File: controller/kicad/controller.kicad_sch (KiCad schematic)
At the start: 28 parts, among them J1 pcie_98, U1 WeAct_STM32H750_Module, U10 ESD5344D, U11 ESD5344D, U12 ESD5344D, U13 ESD5344D, U14 ESD5344D, U15 ESD5344D, U16 ESD5344D, U17 ESD5344D, U18 ESD5344D, U19 ESD5344D, U2 ESD5344D, U20 ESD5344D, U21 ESD5344D, U3 ESD5344D, U4 ESD5344D, U5 ESD5344D, U6 ESD5344D, U7 ESD5344D, U8 ESD5344D, U9 ESD5344D

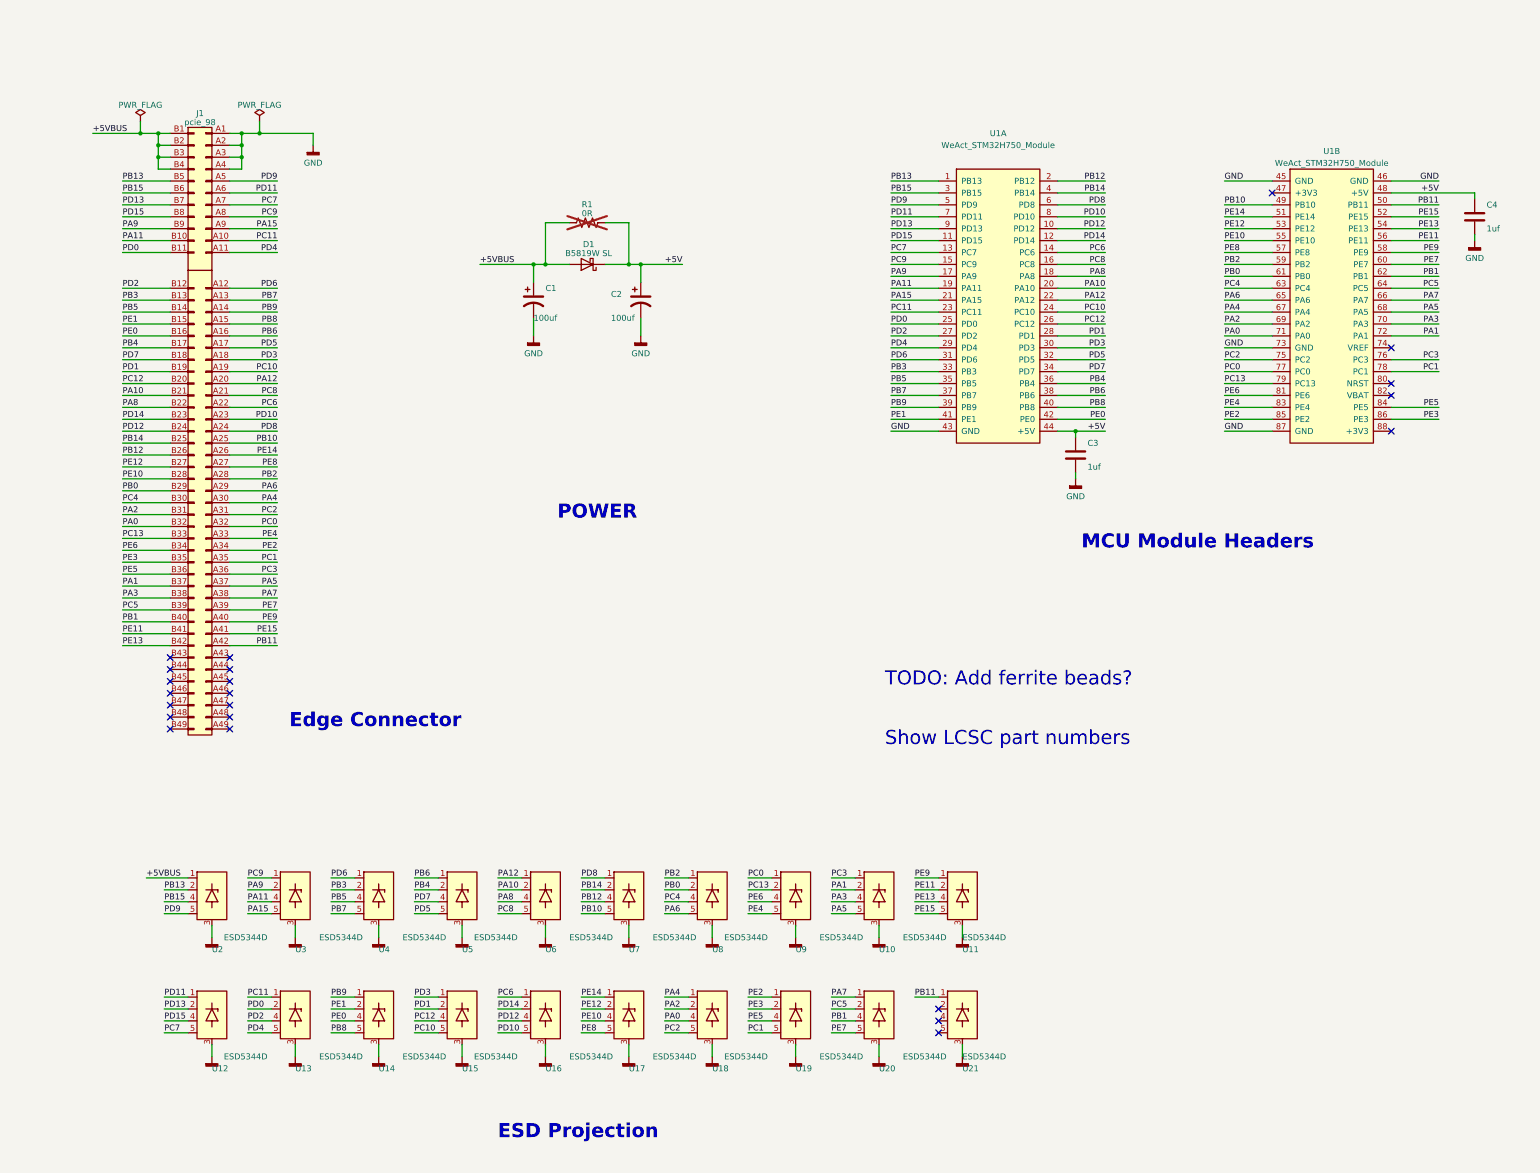
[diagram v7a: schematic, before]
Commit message: Exposed the LCSC numbers in the Controller's schematic.
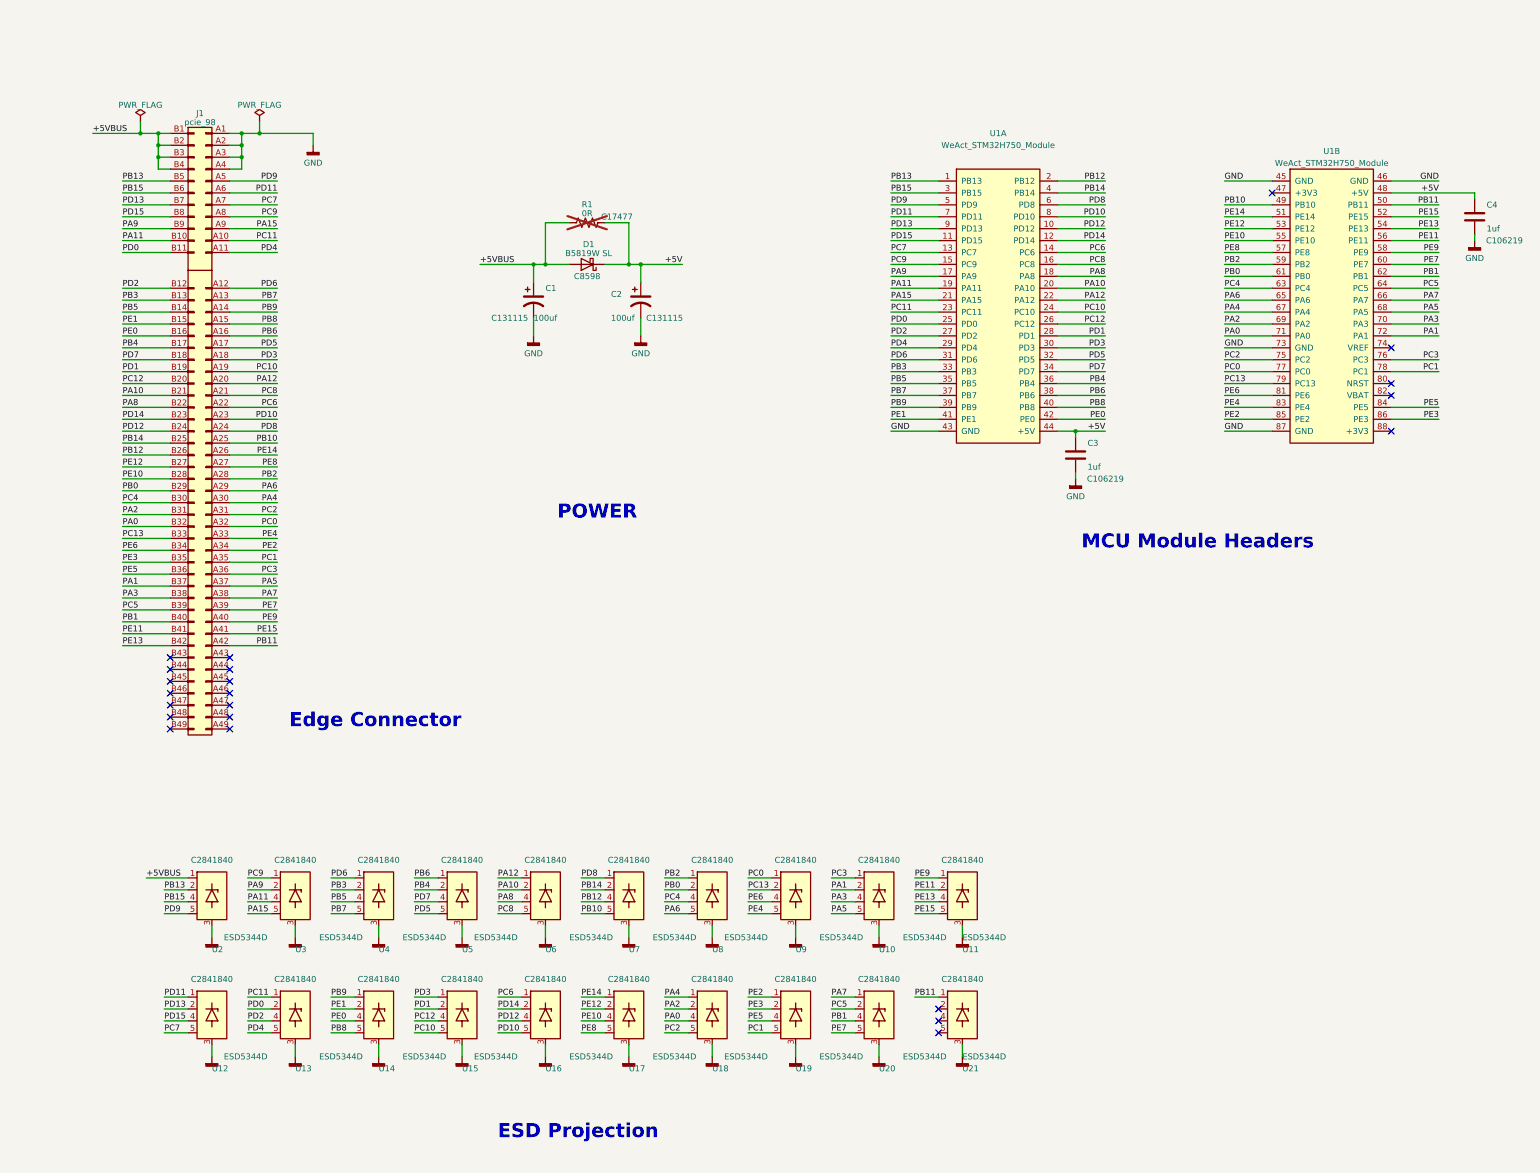
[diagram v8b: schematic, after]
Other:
- note removed: "Show LCSC part numbers"
- note removed: "TODO: Add ferrite beads?"
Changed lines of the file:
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@@
     (effects (font (size 3 3) (thickness 0.6) bold) (justify left bottom))
-  )
-  (text "Show LCSC part numbers" (at 238.76 176.53 0)
-    (effects (font (size 3 3) (color 255 0 0 1)) (justify left bottom))
-  )
-  (text "TODO: Add ferrite beads?" (at 238.76 163.83 0)
-    (effects (font (size 3 3) (color 255 0 0 1)) (justify left bottom))
   )
   (text "MCU Module Headers" (at 280.67 134.62 0)
@@
       (effects (font (size 1.27 1.27)) hide)
     )
-    (property "LCSC" "C2841840" (at 255.27 234.95 0)
-      (effects (font (size 1.27 1.27)) hide)
+    (property "LCSC" "C2841840" (at 255.27 226.06 0)
+      (effects (font (size 1.27 1.27)))
     )
     (pin "1")
@@
       (effects (font (size 1.27 1.27)) hide)
     )
-    (property "LCSC" "C106219" (at 279.4 114.3 0)
-      (effects (font (size 1.27 1.27)) hide)
+    (property "LCSC" "C106219" (at 285.75 119.38 0)
+      (effects (font (size 1.27 1.27)))
     )
     (pin "1")
@@
       (effects (font (size 1.27 1.27)) hide)
     )
-    (property "LCSC" "C2841840" (at 201.93 209.55 0)
-      (effects (font (size 1.27 1.27)) hide)
+    (property "LCSC" "C2841840" (at 201.93 200.66 0)
+      (effects (font (size 1.27 1.27)))
     )
     (pin "1")
@@
       (effects (font (size 1.27 1.27)) hide)
     )
-    (property "LCSC" "C2841840" (at 237.49 234.95 0)
-      (effects (font (size 1.27 1.27)) hide)
+    (property "LCSC" "C2841840" (at 237.49 226.06 0)
+      (effects (font (size 1.27 1.27)))
     )
     (pin "1")
@@
       (effects (font (size 1.27 1.27)) hide)
     )
-    (property "LCSC" "C2841840" (at 219.71 209.55 0)
-      (effects (font (size 1.27 1.27)) hide)
+    (property "LCSC" "C2841840" (at 219.71 200.66 0)
+      (effects (font (size 1.27 1.27)))
     )
     (pin "1")
@@
       (effects (font (size 1.27 1.27)) hide)
     )
-    (property "LCSC" "C2841840" (at 219.71 234.95 0)
-      (effects (font (size 1.27 1.27)) hide)
+    (property "LCSC" "C2841840" (at 219.71 226.06 0)
+      (effects (font (size 1.27 1.27)))
     )
     (pin "1")
@@
       (effects (font (size 1.27 1.27)) hide)
     )
-    (property "LCSC" "C131115" (at 163.83 81.28 0)
-      (effects (font (size 1.27 1.27)) hide)
+    (property "LCSC" "C131115" (at 158.75 85.09 0)
+      (effects (font (size 1.27 1.27)))
     )
     (pin "1")
@@
       (effects (font (size 1.27 1.27)) hide)
     )
-    (property "LCSC" "C2841840" (at 113.03 209.55 0)
-      (effects (font (size 1.27 1.27)) hide)
+    (property "LCSC" "C2841840" (at 113.03 200.66 0)
+      (effects (font (size 1.27 1.27)))
     )
     (pin "1")
@@
       (effects (font (size 1.27 1.27)) hide)
     )
-    (property "LCSC" "C2841840" (at 201.93 234.95 0)
-      (effects (font (size 1.27 1.27)) hide)
+    (property "LCSC" "C2841840" (at 201.93 226.06 0)
+      (effects (font (size 1.27 1.27)))
     )
     (pin "1")
@@
       (effects (font (size 1.27 1.27)) hide)
     )
-    (property "LCSC" "C2841840" (at 255.27 209.55 0)
-      (effects (font (size 1.27 1.27)) hide)
+    (property "LCSC" "C2841840" (at 255.27 200.66 0)
+      (effects (font (size 1.27 1.27)))
     )
     (pin "1")
@@
       (effects (font (size 1.27 1.27)) hide)
     )
-    (property "LCSC" "C2841840" (at 95.25 209.55 0)
-      (effects (font (size 1.27 1.27)) hide)
+    (property "LCSC" "C2841840" (at 95.25 200.66 0)
+      (effects (font (size 1.27 1.27)))
     )
     (pin "1")
@@
       (effects (font (size 1.27 1.27)) hide)
     )
-    (property "LCSC" "C2841840" (at 95.25 234.95 0)
-      (effects (font (size 1.27 1.27)) hide)
+    (property "LCSC" "C2841840" (at 95.25 226.06 0)
+      (effects (font (size 1.27 1.27)))
     )
     (pin "1")
@@
       (effects (font (size 1.27 1.27)) hide)
     )
-    (property "LCSC" "C2841840" (at 184.15 209.55 0)
-      (effects (font (size 1.27 1.27)) hide)
+    (property "LCSC" "C2841840" (at 184.15 200.66 0)
+      (effects (font (size 1.27 1.27)))
     )
     (pin "1")
@@
   )
   (symbol (lib_id "Device:D_Schottky") (at 175.26 73.66 180) (unit 1)
-    (in_bom yes) (on_board yes) (dnp no) (fields_autoplaced)
+    (in_bom yes) (on_board yes) (dnp no)
     (property "Reference" "D1" (at 175.5775 69.3801 0)
       (effects (font (size 1.27 1.27)))
@@
       (effects (font (size 1.27 1.27)) hide)
     )
-    (property "LCSC" "C8598" (at 175.26 73.66 0)
-      (effects (font (size 1.27 1.27)) hide)
+    (property "LCSC" "C8598" (at 175.26 76.2 0)
+      (effects (font (size 1.27 1.27)))
     )
     (pin "1")
@@
       (effects (font (size 1.27 1.27)) hide)
     )
-    (property "LCSC" "C2841840" (at 237.49 209.55 0)
-      (effects (font (size 1.27 1.27)) hide)
+    (property "LCSC" "C2841840" (at 237.49 200.66 0)
+      (effects (font (size 1.27 1.27)))
     )
     (pin "1")
@@
       (effects (font (size 1.27 1.27)) hide)
     )
-    (property "LCSC" "C2841840" (at 130.81 209.55 0)
-      (effects (font (size 1.27 1.27)) hide)
+    (property "LCSC" "C2841840" (at 130.81 200.66 0)
+      (effects (font (size 1.27 1.27)))
     )
     (pin "1")
@@
       (effects (font (size 1.27 1.27)) hide)
     )
-    (property "LCSC" "C106219" (at 364.49 63.5 0)
-      (effects (font (size 1.27 1.27)) hide)
+    (property "LCSC" "C106219" (at 370.84 68.58 0)
+      (effects (font (size 1.27 1.27)))
     )
     (pin "1")
@@
       (effects (font (size 1.27 1.27)) hide)
     )
-    (property "LCSC" "C2841840" (at 113.03 234.95 0)
-      (effects (font (size 1.27 1.27)) hide)
+    (property "LCSC" "C2841840" (at 113.03 226.06 0)
+      (effects (font (size 1.27 1.27)))
     )
     (pin "1")
@@
       (effects (font (size 1.27 1.27)) hide)
     )
-    (property "LCSC" "C2841840" (at 148.59 234.95 0)
-      (effects (font (size 1.27 1.27)) hide)
+    (property "LCSC" "C2841840" (at 148.59 226.06 0)
+      (effects (font (size 1.27 1.27)))
     )
     (pin "1")
@@
       (effects (font (size 1.27 1.27)) hide)
     )
-    (property "LCSC" "C2841840" (at 148.59 209.55 0)
-      (effects (font (size 1.27 1.27)) hide)
+    (property "LCSC" "C2841840" (at 148.59 200.66 0)
+      (effects (font (size 1.27 1.27)))
     )
     (pin "1")
@@
       (effects (font (size 1.27 1.27)) hide)
     )
-    (property "LCSC" "C2841840" (at 130.81 234.95 0)
-      (effects (font (size 1.27 1.27)) hide)
+    (property "LCSC" "C2841840" (at 130.81 226.06 0)
+      (effects (font (size 1.27 1.27)))
     )
     (pin "1")
@@
   )
   (symbol (lib_id "Device:R_US") (at 175.26 64.77 90) (unit 1)
-    (in_bom no) (on_board yes) (dnp yes) (fields_autoplaced)
+    (in_bom no) (on_board yes) (dnp yes)
     (property "Reference" "R1" (at 175.26 60.8711 90)
       (effects (font (size 1.27 1.27)))
@@
       (effects (font (size 1.27 1.27)) hide)
     )
-    (property "LCSC" "C17477" (at 175.26 64.77 90)
-      (effects (font (size 1.27 1.27)) hide)
+    (property "LCSC" "C17477" (at 181.61 63.5 90)
+      (effects (font (size 1.27 1.27)))
     )
     (pin "1")
@@
       (effects (font (size 1.27 1.27)) hide)
     )
-    (property "LCSC" "C2841840" (at 184.15 234.95 0)
-      (effects (font (size 1.27 1.27)) hide)
+    (property "LCSC" "C2841840" (at 184.15 226.06 0)
+      (effects (font (size 1.27 1.27)))
     )
     (pin "1")
@@
       (effects (font (size 1.27 1.27)) hide)
     )
-    (property "LCSC" "C2841840" (at 166.37 234.95 0)
-      (effects (font (size 1.27 1.27)) hide)
+    (property "LCSC" "C2841840" (at 166.37 226.06 0)
+      (effects (font (size 1.27 1.27)))
     )
     (pin "1")
@@
       (effects (font (size 1.27 1.27)) hide)
     )
-    (property "LCSC" "C131115" (at 186.69 81.28 0)
-      (effects (font (size 1.27 1.27)) hide)
+    (property "LCSC" "C131115" (at 191.77 85.09 0)
+      (effects (font (size 1.27 1.27)))
     )
     (pin "1")
@@
       (effects (font (size 1.27 1.27)) hide)
     )
-    (property "LCSC" "C2841840" (at 166.37 209.55 0)
-      (effects (font (size 1.27 1.27)) hide)
-    )
-    (pin "1")
+    (property "LCSC" "C2841840" (at 166.37 200.66 0)
+      (effects (font (size 1.27 1.27)))
+    )
+    (pin "1")
